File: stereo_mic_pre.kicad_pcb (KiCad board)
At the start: 2 copper layers, 69 x 33 mm, 46 parts, among them J1 AudioJack3, J2 AudioJack3, Q1 Si2312BDS, SW1 SW_SPDT, U1 TLE2426xP, U2 TPS7250, U3 OPA1612AxD

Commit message: Changed D2 and D3 to smaller 0603 diode, changed and rerouted for 4 layers
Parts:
- D2, D3: value SMBJ5.0A-TP -> CG0603MLC-05E; footprint Diode_SMD:D_SMB_Handsoldering -> Diode_SMD:D_0603_1608Metric_Pad1.05x0.95mm_HandSolder
- moved R10 6.31 mm to (214.6, 109.5), turned to 180 degrees
- moved R9 5.00 mm to (214.6, 100.8), turned to 180 degrees
- moved D3 4.54 mm to (214.6, 107.8), turned to 0 degrees
- moved D2 3.56 mm to (214.6, 102.5), turned to 0 degrees
- moved C12 1.35 mm to (222.0, 110.0)
- moved R16 1.35 mm to (223.8, 110.0)
- moved C10 0.90 mm to (217.2, 105.0)
- moved C11 0.90 mm to (224.5, 99.0)
- moved C13 0.90 mm to (226.0, 105.8)
- moved R11 0.90 mm to (222.5, 99.0)
- moved R12 0.90 mm to (220.8, 99.0)
- moved R13 0.90 mm to (218.5, 110.0)
- moved R14 0.90 mm to (220.2, 110.0)
- moved R15 0.90 mm to (226.2, 99.0)
- moved U3 0.90 mm to (221.8, 104.5)
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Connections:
- net +4V5 renamed VDD_VIRT
- net Earth renamed -4V5
- net GND renamed GND_VIRT
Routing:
- net -4V5: track 48.4 -> 2.63 mm, vias 9 -> 0
- net VDD_VIRT: track 92.4 -> 55.0 mm, vias 4 -> 3
- net /amplifier/IN_R: track 26.9 -> 15.3 mm
- net /amplifier/IN_L: track 27.5 -> 17.0 mm
- net Net-(C12-Pad2): track 36.3 -> 29.3 mm
- net Net-(C11-Pad2): track 48.5 -> 44.4 mm
- net GND_VIRT: track 16.9 -> 14.9 mm, vias 1 -> 6
- net Net-(RV1A-7): track 19.8 -> 18.2 mm
- net Net-(C8-Pad1): track 22.1 -> 20.7 mm
- net /power/V_BAT: track 77.4 -> 76.6 mm
- net Net-(U3B--): track 7.31 -> 6.81 mm
- added copper zone on In2.Cu, net GND_VIRT
- added copper zone on In1.Cu, net VDD_VIRT
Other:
- copper layers 2 -> 4

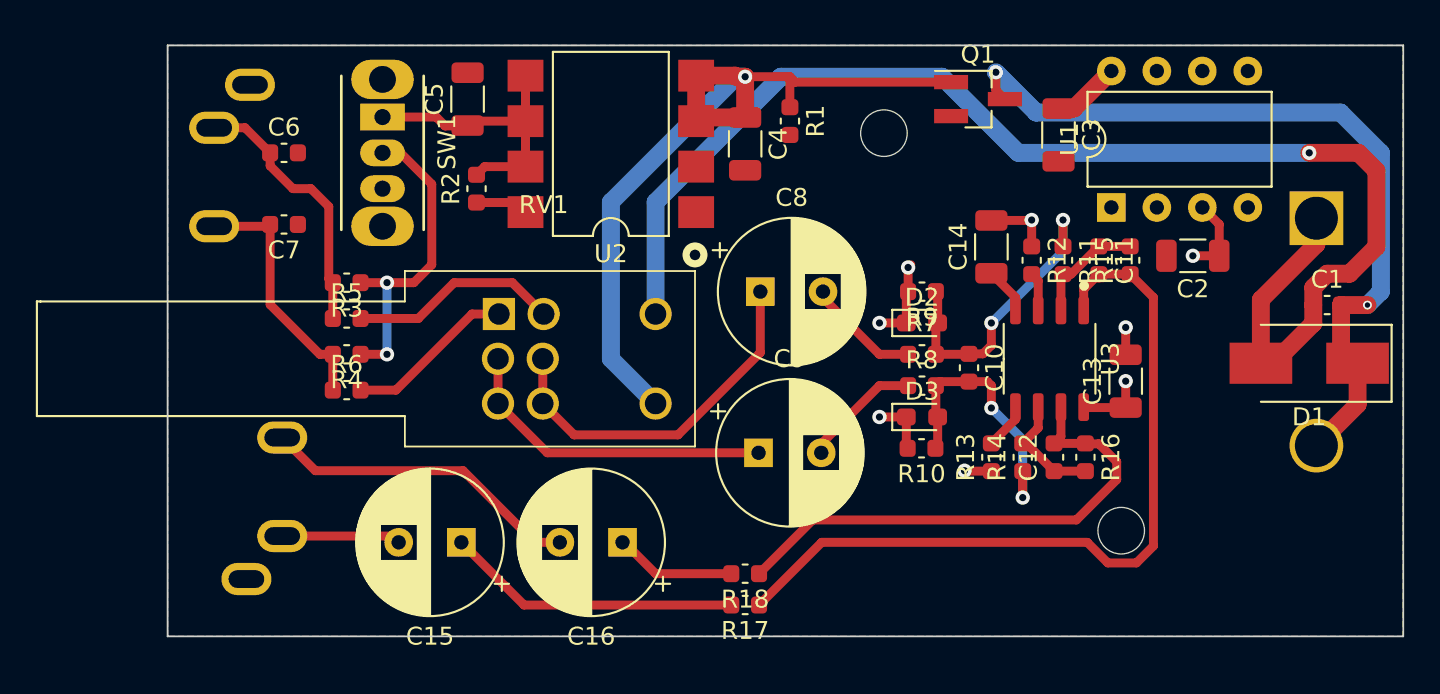
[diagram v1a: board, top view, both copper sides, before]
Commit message: Finished placing refdes, fix DRC errors
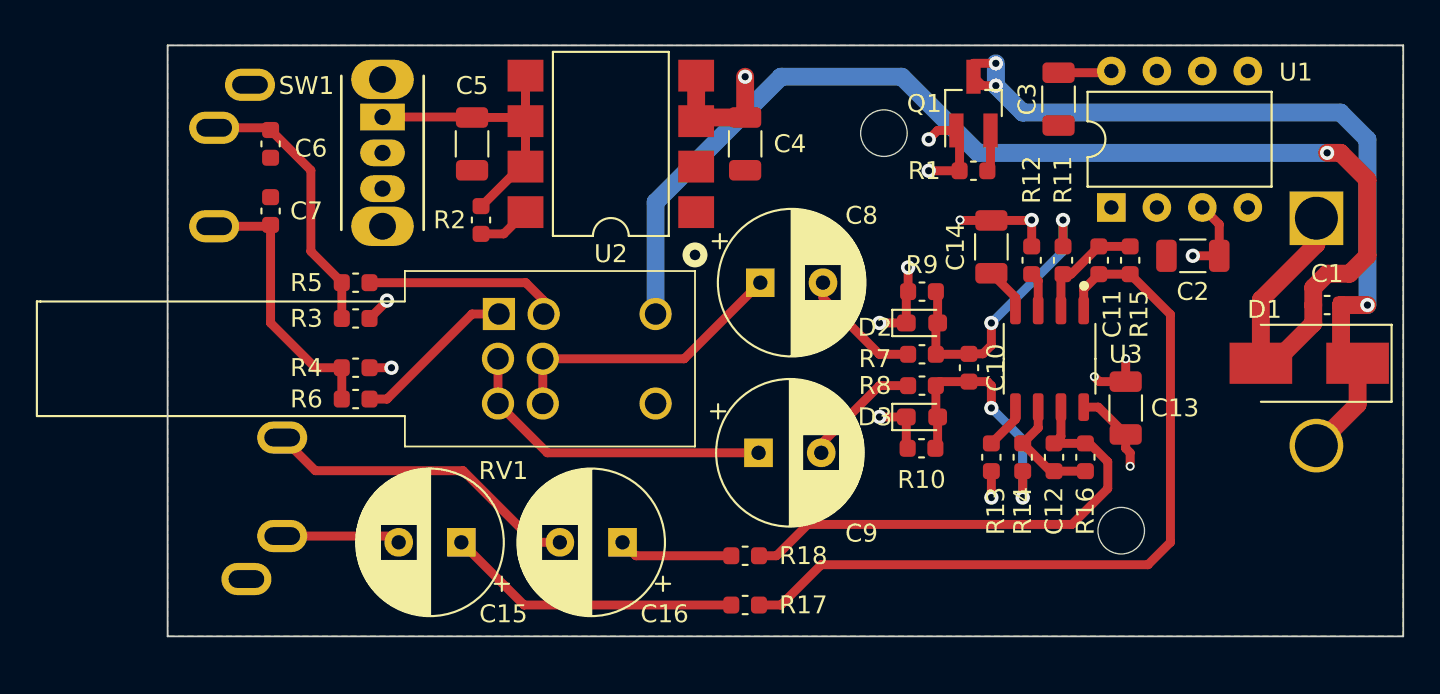
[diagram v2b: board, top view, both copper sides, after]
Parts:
- moved R1 10.6 mm to (217.5, 94.0), turned to 0 degrees
- moved C5 2.51 mm to (189.5, 92.5), turned to -90 degrees
- moved R3 2.06 mm to (183.0, 102.2)
- moved R5 2.06 mm to (183.0, 100.2)
- moved C3 2.00 mm to (222.2, 90.0)
- moved R2 1.77 mm to (190.0, 96.8)
- moved C13 1.50 mm to (226.0, 107.2)
- moved C7 1.06 mm to (178.2, 96.2), turned to -90 degrees
- moved R18 1.00 mm to (204.8, 115.5)
- moved C6 0.90 mm to (178.2, 92.5), turned to -90 degrees
- moved R4 0.90 mm to (183.0, 105.0)
- moved R6 0.71 mm to (183.0, 106.8)
- moved C8 0.50 mm to (205.6, 100.2)
- moved Q1 0.35 mm to (217.5, 90.2), turned to 90 degrees
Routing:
- net VDD_VIRT: track 55.0 -> 22.9 mm, vias 3 -> 5
- net Net-(C8-Pad1): track 20.7 -> 16.4 mm
- net GND_VIRT: track 14.9 -> 18.0 mm, vias 6 -> 8
- net -4V5: track 2.63 -> 4.95 mm
- net /power/GND_BAT: track 44.5 -> 46.6 mm, vias 2 -> 3
- net /power/V_BAT: track 76.6 -> 75.2 mm
- net /audio_in/IN_R: track 14.3 -> 15.4 mm
- net Net-(C12-Pad2): track 29.3 -> 28.1 mm
- net Net-(R5-Pad2): track 11.8 -> 10.9 mm
- net Net-(U1-NOISE_REDUCTION): track 3.82 -> 2.99 mm
- net Net-(SW1-B): track 17.8 -> 18.4 mm
